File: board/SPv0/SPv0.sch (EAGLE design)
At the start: 2 parts, among them IC1 S34ML0XG1, IC2 S34ML0XG1

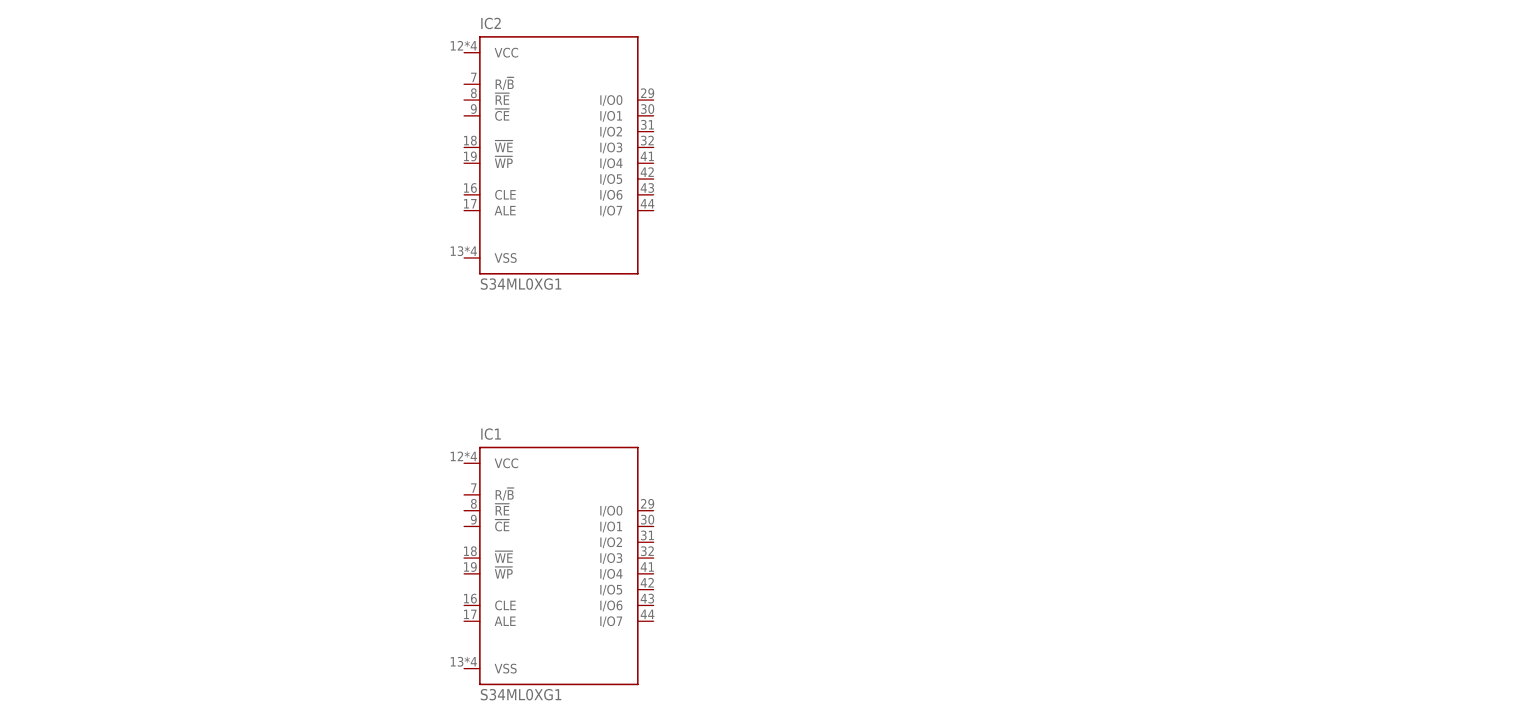
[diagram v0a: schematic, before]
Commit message: added uC, xtal, decoupling caps for uC, usb lines/power
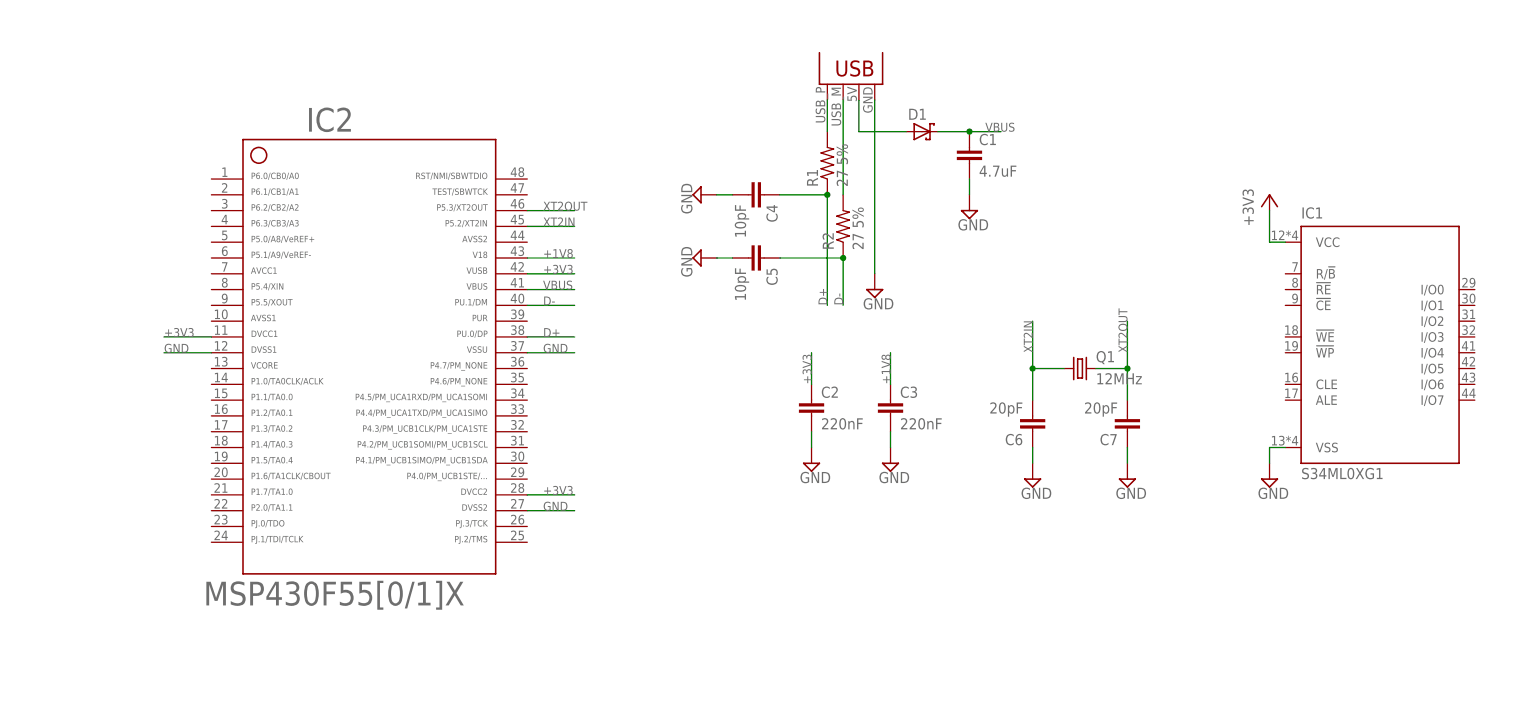
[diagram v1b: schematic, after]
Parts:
- added C1: 4.7uF, rcl:C-EUC0805
- added C2, C3: 220nF, rcl:C-EUC0805
- added C4, C5: 10pF, rcl:C-EUC0805
- added C6, C7: 20pF, rcl:C-EUC0805
- added D1: (no value), diode:SCHOTTKY-DIODESMD
- added JP1: USBPCB, SparkFun-Connectors:USBPCB
- added Q1: 12MHz, crystal:CRYSTALHC49UP
- added R1, R2: 27 5%, rcl:R-US_R0805
- IC2: value S34ML0XG1 -> F55[0/1]X---PT48; device Flash:S34ML0XG1 -> TI_MSP430_v16:F55[0/1]X---PT48
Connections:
- new net +1V8: C3.1, IC2.43
- new net +3V3: C2.1, IC1.VCC, IC2.11, IC2.28, IC2.42
- new net D+: C4.1, IC2.38, R1.1
- new net D-: C5.1, IC2.40, R2.1
- new net GND: C1.2, C2.2, C3.2, C4.2, C5.2, C6.1, C7.1, IC1.VSS, IC2.12, IC2.27, IC2.37, JP1.GND
- new net N$1: JP1.D+, R1.2
- new net N$2: JP1.D-, R2.2
- new net N$3: D1.A, JP1.VBUS
- new net VBUS: C1.1, D1.C, IC2.41
- new net XT2IN: C6.2, IC2.45, Q1.1
- new net XT2OUT: C7.2, IC2.46, Q1.2
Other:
- moved on the sheet: IC1

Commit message: added crystal footprint; added to schematic
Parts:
- Q1: device crystal:CRYSTALHC49UP -> Passives:CRYSTAL
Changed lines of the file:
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@@
 <part name="R2" library="rcl" deviceset="R-US_" device="R0805" value="27 5%"/>
 <part name="D1" library="diode" deviceset="SCHOTTKY-DIODE" device="SMD"/>
-<part name="Q1" library="crystal" deviceset="CRYSTAL" device="HC49UP" value="12MHz"/>
+<part name="Q1" library="Passives" deviceset="CRYSTAL" device="" value="12MHz"/>
 </parts>
 <sheets>

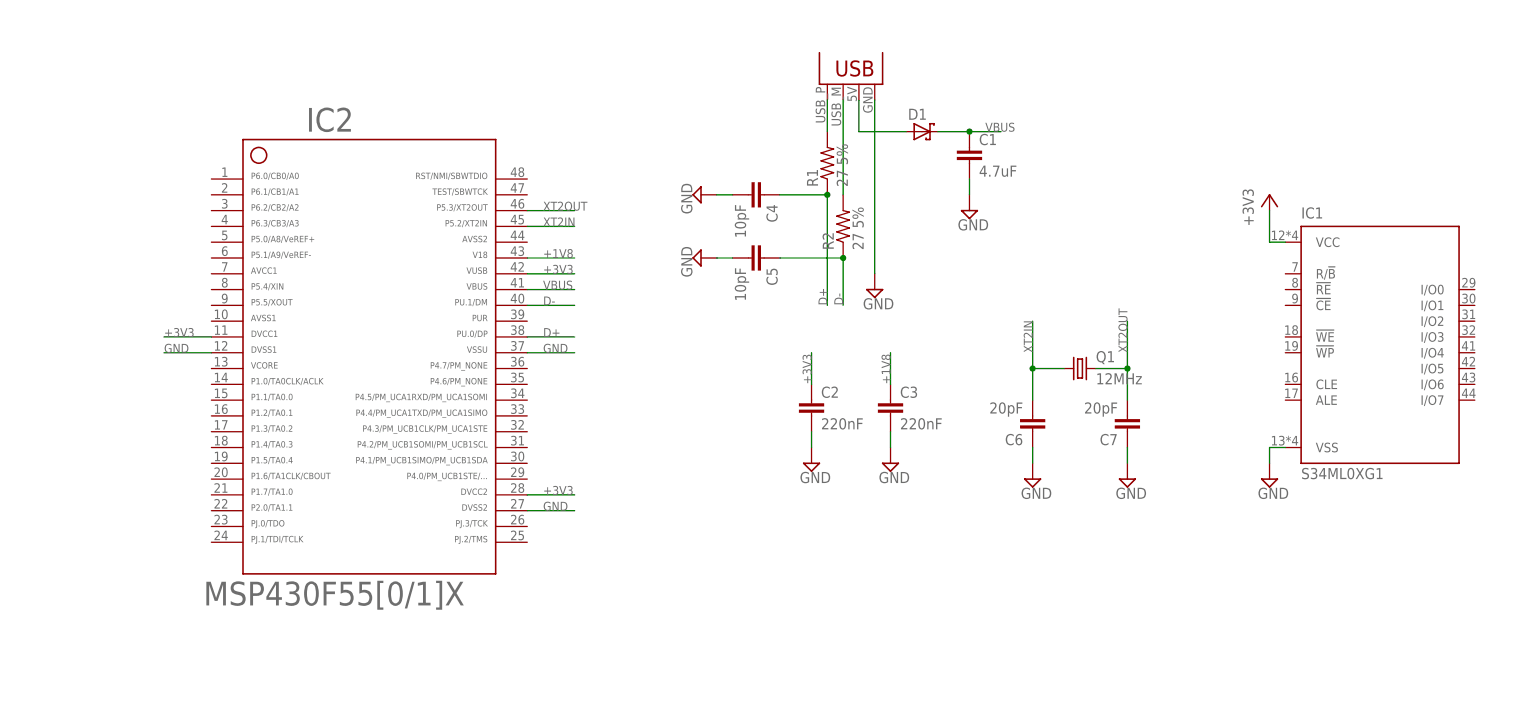
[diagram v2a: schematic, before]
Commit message: added switch to passives library added BSL reset switch added jtag header
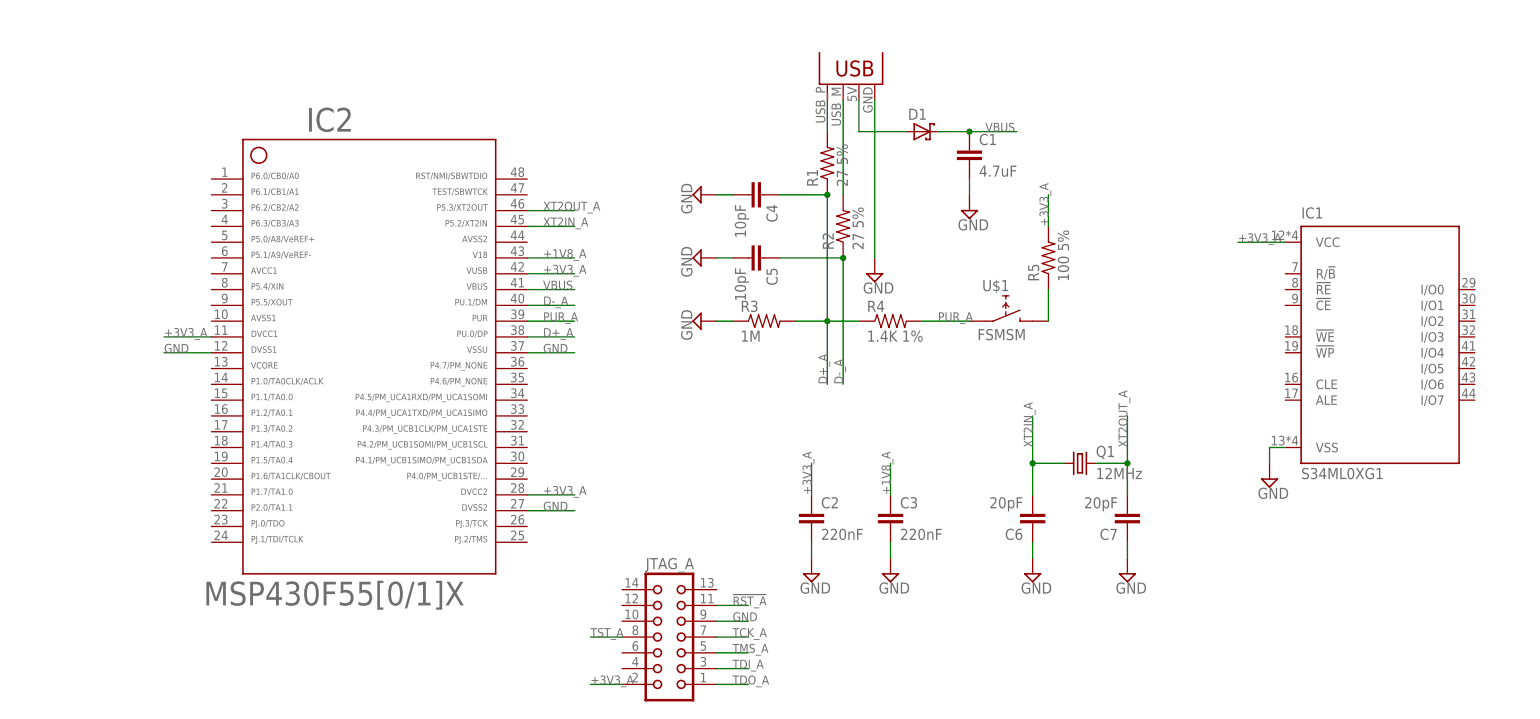
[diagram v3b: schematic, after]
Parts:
- added JTAG_A: (no value), con-harting:CON14
- added R3: 1M, rcl:R-US_R0805
- added R4: 1.4K 1%, rcl:R-US_R0805
- added R5: 100 5%, rcl:R-US_R0805
- added U$1: FSMSM, Passives:FSMSM
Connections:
- net +1V8 renamed +1V8_A
- net D- renamed D-_A
- net XT2IN renamed XT2IN_A
- net XT2OUT renamed XT2OUT_A
- removed net +3V3: C2.1, IC1.VCC, IC2.11, IC2.28, IC2.42
- removed net D+: C4.1, IC2.38, R1.1
- new net !RST_A!: JTAG_A.11
- new net +3V3_A: C2.1, IC1.VCC, IC2.11, IC2.28, IC2.42, JTAG_A.2, R5.2
- new net D+_A: C4.1, IC2.38, R1.1, R3.2, R4.1
- new net N$4: R5.1, U$1.B
- new net PUR_A: IC2.39, R4.2, U$1.A1
- new net TCK_A: JTAG_A.7
- new net TDI_A: JTAG_A.3
- new net TDO_A: JTAG_A.1
- new net TMS_A: JTAG_A.5
- new net TST_A: JTAG_A.8
- net GND: now also JTAG_A.9, R3.1
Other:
- moved on the sheet: C2, C3, C6, C7, Q1
